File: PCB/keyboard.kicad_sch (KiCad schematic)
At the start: 1 part, among them U1 Pico

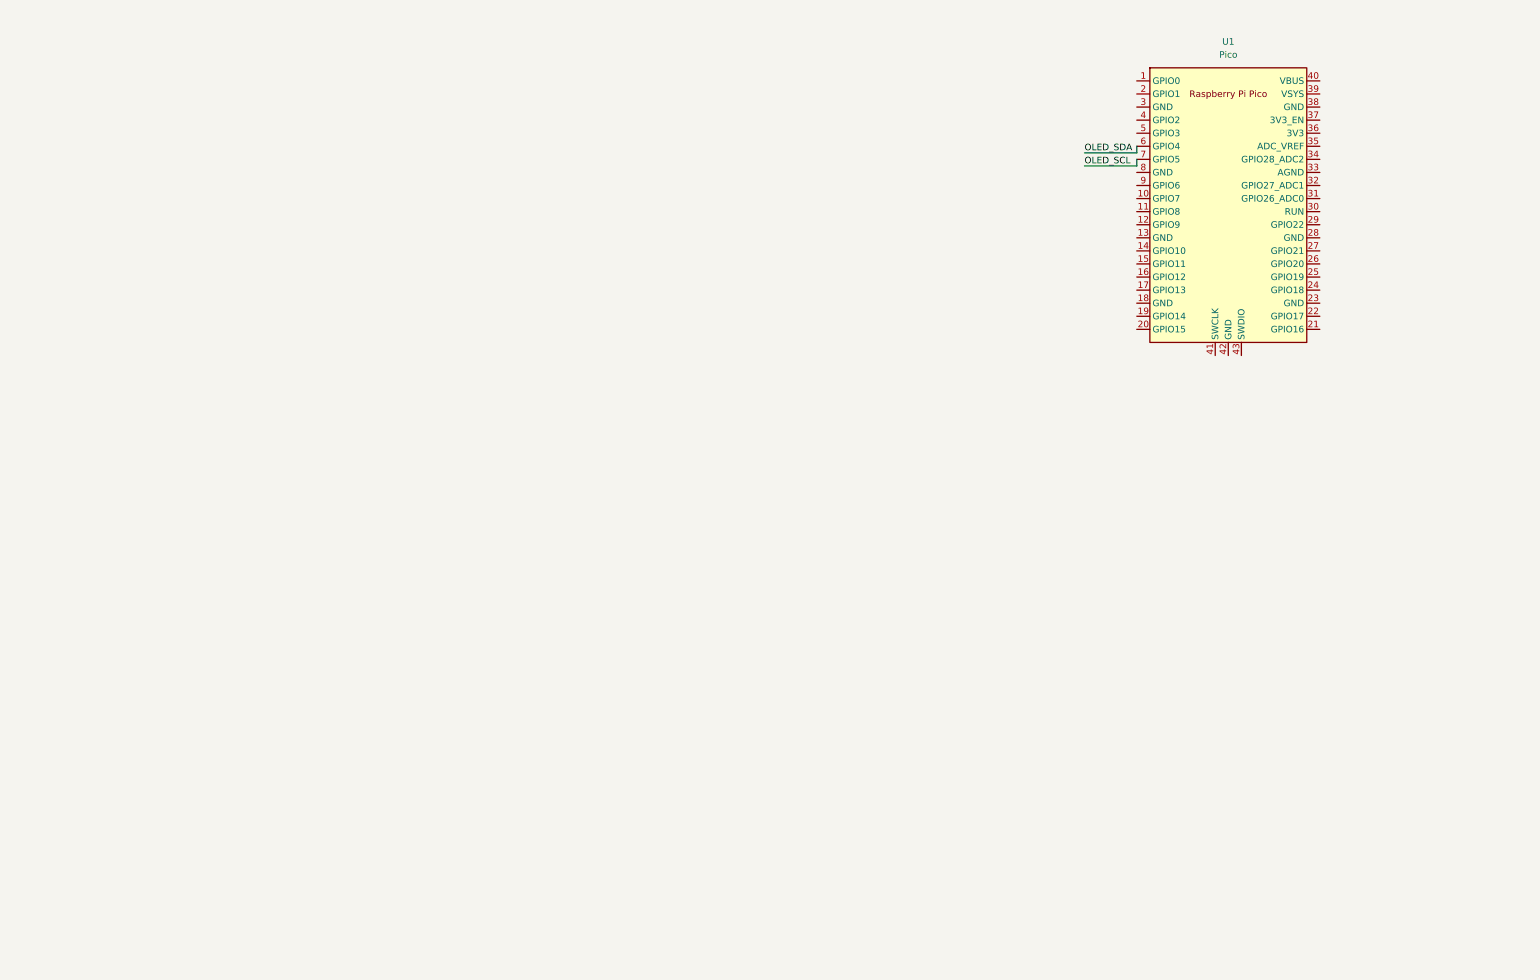
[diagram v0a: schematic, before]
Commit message: Major PCB Updates (Read desc.)
Since the last update, I designed an ANSI TKL based keyboard layout schematic in KiCad using a Raspberry Pi Pico 2W as the controller. I started by selecting and labeling usable GPIO pins on the Pico and assigning them to six row lines (ROW0–ROW5) and fifteen column lines (COL0–COL14). I had some issues figuring out diode orientation, but I got it eventually. I then expanded it into a full ANSI-based TKL layout.
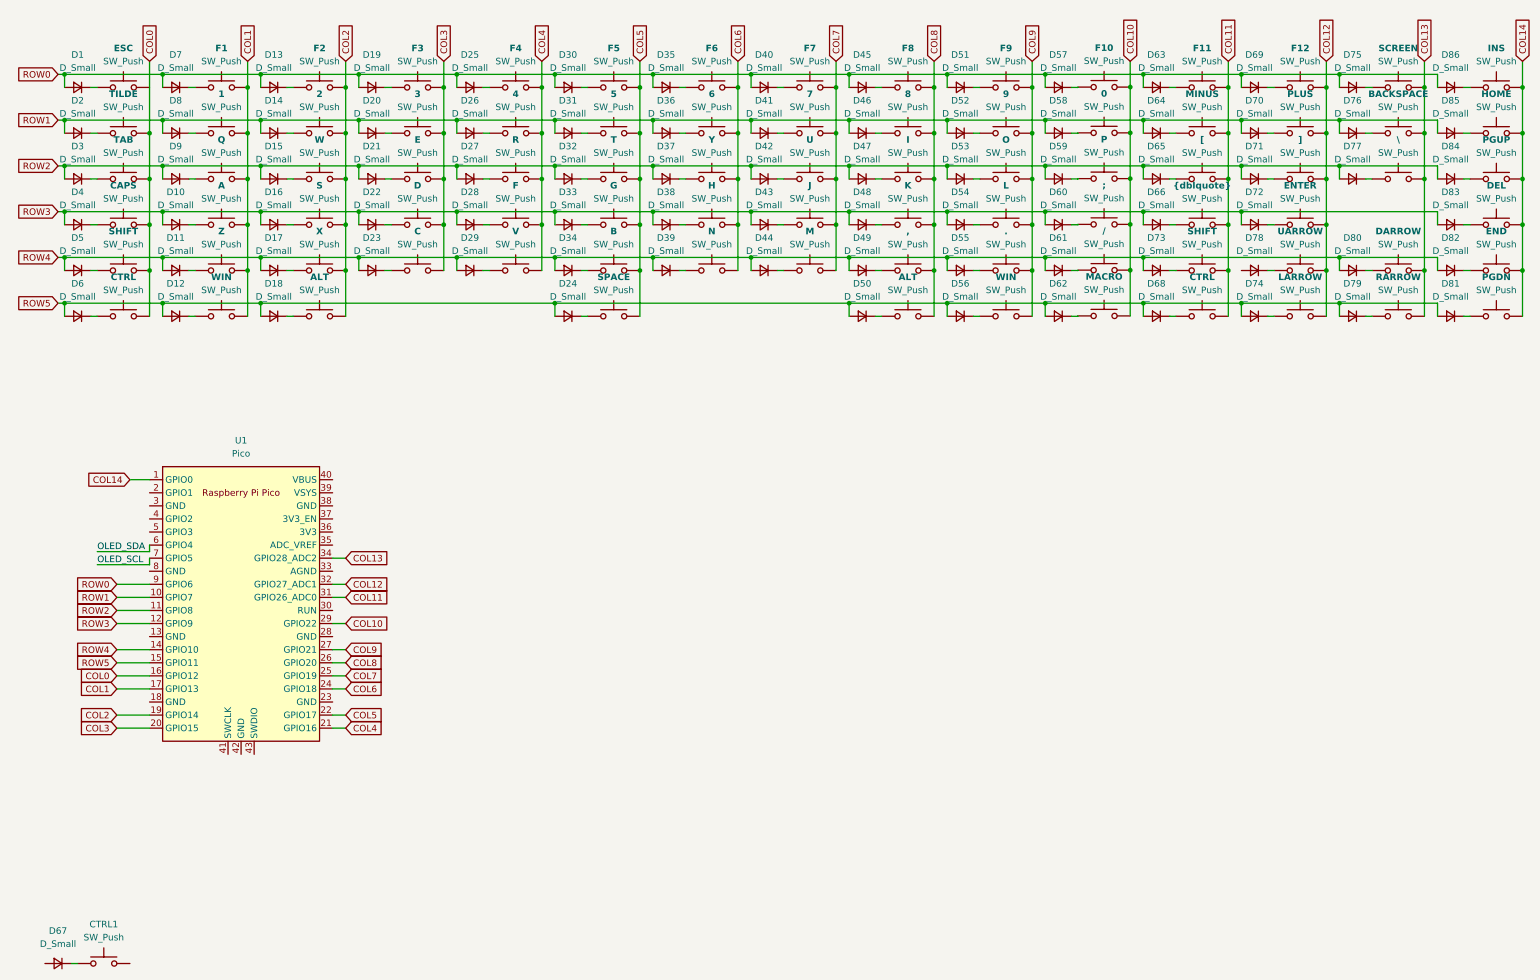
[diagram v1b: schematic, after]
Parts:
- added ,, ., /, 0, 1, 2, 3, 4, 5, 6, 7, 8, 9, ;, A, ALT (x2), B, BACKSPACE, C, CAPS, CTRL (x2), CTRL1, D, DARROW, DEL, E, END, ENTER, ESC, F, F1, F10, F11, F12, F2, F3, F4, F5, F6, F7, F8, F9, G, H, HOME, I, INS, J, K, L, LARROW, M, MACRO, MINUS, N, O, P, PGDN, PGUP, PLUS, Q, R, RARROW, S, SCREEN, SHIFT (x2), SPACE, T, TAB, TILDE, U, UARROW, V, W, WIN (x2), X, Y, Z, [, \, ], {dblquote}: SW_Push, symbol Switch:SW_Push
- added D1, D10, D11, D12, D13, D14, D15, D16, D17, D18, D19, D2, D20, D21, D22, D23, D24, D25, D26, D27, D28, D29, D3, D30, D31, D32, D33, D34, D35, D36, D37, D38, D39, D4, D40, D41, D42, D43, D44, D45, D46, D47, D48, D49, D5, D50, D51, D52, D53, D54, D55, D56, D57, D58, D59, D6, D60, D61, D62, D63, D64, D65, D66, D67, D68, D69, D7, D70, D71, D72, D73, D74, D75, D76, D77, D78, D79, D8, D80, D81, D82, D83, D84, D85, D86, D9: D_Small, symbol Device:D_Small
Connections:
- net COL14: now reaches U1.1 (GPIO0)
- net COL14: now also DEL.2, END.2, HOME.2, INS.2, PGDN.2, PGUP.2
- net ROW1: now reaches U1.10 (GPIO7)
- net ROW1: now also D14.2 (A), D2.2 (A), D20.2 (A), D26.2 (A), D31.2 (A), D36.2 (A), D41.2 (A), D46.2 (A), D52.2 (A), D58.2 (A), D64.2 (A), D70.2 (A), D76.2 (A), D8.2 (A), D85.2 (A)
- net ROW2: now reaches U1.11 (GPIO8)
- net ROW2: now also D15.2 (A), D21.2 (A), D27.2 (A), D3.2 (A), D32.2 (A), D37.2 (A), D42.2 (A), D47.2 (A), D53.2 (A), D59.2 (A), D65.2 (A), D71.2 (A), D77.2 (A), D84.2 (A), D9.2 (A)
- net ROW3: now reaches U1.12 (GPIO9)
- net ROW3: now also D10.2 (A), D16.2 (A), D22.2 (A), D28.2 (A), D33.2 (A), D38.2 (A), D4.2 (A), D43.2 (A), D48.2 (A), D54.2 (A), D60.2 (A), D66.2 (A), D72.2 (A), D83.2 (A)
- net ROW4: now reaches U1.14 (GPIO10)
- net ROW4: now also D11.2 (A), D17.2 (A), D23.2 (A), D29.2 (A), D34.2 (A), D39.2 (A), D44.2 (A), D49.2 (A), D5.2 (A), D55.2 (A), D61.2 (A), D73.2 (A), D80.2 (A), D82.2 (A)
- net ROW5: now reaches U1.15 (GPIO11)
- net ROW5: now also D12.2 (A), D18.2 (A), D24.2 (A), D50.2 (A), D56.2 (A), D6.2 (A), D62.2 (A), D68.2 (A), D74.2 (A), D79.2 (A), D81.2 (A)
- net COL0: now reaches U1.16 (GPIO12)
- net COL0: now also CAPS.2, CTRL.2, SHIFT.2, TAB.2, TILDE.2
- net COL1: now reaches U1.17 (GPIO13)
- net COL1: now also 1.2, A.2, F1.2, Q.2, WIN.2, Z.2
- net COL2: now reaches U1.19 (GPIO14)
- net COL2: now also 2.2, ALT.2, F2.2, S.2, W.2, X.2
- net COL3: now reaches U1.20 (GPIO15)
- net COL3: now also 3.2, C.2, D.2, E.2, F3.2
- net COL4: now reaches U1.21 (GPIO16)
- net COL4: now also 4.2, F.2, F4.2, R.2, V.2
- net COL5: now reaches U1.22 (GPIO17)
- net COL5: now also 5.2, B.2, F5.2, G.2, SPACE.2, T.2
- net COL6: now reaches U1.24 (GPIO18)
- net COL6: now also 6.2, F6.2, H.2, N.2, Y.2
- net COL7: now reaches U1.25 (GPIO19)
- net COL7: now also 7.2, F7.2, J.2, M.2, U.2
- net COL8: now reaches U1.26 (GPIO20)
- net COL8: now also ,.2, 8.2, ALT.2, F8.2, I.2, K.2
- net COL9: now reaches U1.27 (GPIO21)
- net COL9: now also ..2, 9.2, F9.2, L.2, O.2, WIN.2
- net COL10: now reaches U1.29 (GPIO22)
- net COL10: now also /.2, 0.2, ;.2, F10.2, MACRO.2, P.2
- net COL11: now reaches U1.31 (GPIO26_ADC0)
- net COL11: now also CTRL.2, F11.2, MINUS.2, SHIFT.2, [.2, {dblquote}.2
- net COL12: now reaches U1.32 (GPIO27_ADC1)
- net COL12: now also ENTER.2, F12.2, LARROW.2, PLUS.2, UARROW.2, ].2
- net COL13: now reaches U1.34 (GPIO28_ADC2)
- net COL13: now also BACKSPACE.2, DARROW.2, RARROW.2, SCREEN.2, \.2
- net ROW0: now reaches U1.9 (GPIO6)
- net ROW0: now also D1.2 (A), D13.2 (A), D19.2 (A), D25.2 (A), D30.2 (A), D35.2 (A), D40.2 (A), D45.2 (A), D51.2 (A), D57.2 (A), D63.2 (A), D69.2 (A), D7.2 (A), D75.2 (A), D86.2 (A)
- new net: D37.1 (K), Y.1
- new net: D33.1 (K), G.1
- new net: D35.1 (K), F6.1
- new net: 8.1, D46.1 (K)
- new net: D25.1 (K), F4.1
- new net: D69.1 (K), F12.1
- new net: A.1, D10.1 (K)
- new net: D86.1 (K), INS.1
- new net: 4.1, D26.1 (K)
- new net: D43.1 (K), J.1
- new net: D44.1 (K), M.1
- new net: D74.1 (K), LARROW.1
- new net: D62.1 (K), MACRO.1
- new net: D85.1 (K), HOME.1
- new net: D71.1 (K), ].1
- new net: D30.1 (K), F5.1
- new net: D51.1 (K), F9.1
- new net: D12.1 (K), WIN.1
- new net: D15.1 (K), W.1
- new net: D39.1 (K), N.1
- new net: CAPS.1, D4.1 (K)
- new net: D47.1 (K), I.1
- new net: D84.1 (K), PGUP.1
- new net: 7.1, D41.1 (K)
- new net: 2.1, D14.1 (K)
- new net: D21.1 (K), E.1
- new net: D28.1 (K), F.1
- new net: D59.1 (K), P.1
- new net: D40.1 (K), F7.1
- new net: D53.1 (K), O.1
- new net: D73.1 (K), SHIFT.1
- new net: D75.1 (K), SCREEN.1
- new net: 6.1, D36.1 (K)
- new net: ..1, D55.1 (K)
- new net: D81.1 (K), PGDN.1
- new net: D13.1 (K), F2.1
- new net: ALT.1, D18.1 (K)
- new net: D17.1 (K), X.1
- new net: CTRL1.1, D67.1 (K)
- new net: D29.1 (K), V.1
- new net: D57.1 (K), F10.1
- new net: BACKSPACE.1, D76.1 (K)
- new net: CTRL.1, D6.1 (K)
- new net: D3.1 (K), TAB.1
- new net: D65.1 (K), [.1
- new net: D63.1 (K), F11.1
- new net: D64.1 (K), MINUS.1
- new net: D5.1 (K), SHIFT.1
- new net: D72.1 (K), ENTER.1
- new net: D32.1 (K), T.1
- new net: D80.1 (K), DARROW.1
- new net: D77.1 (K), \.1
- new net: ALT.1, D50.1 (K)
- new net: /.1, D61.1 (K)
- new net: D42.1 (K), U.1
- new net: D79.1 (K), RARROW.1
- new net: D82.1 (K), END.1
- new net: ;.1, D60.1 (K)
- new net: D48.1 (K), K.1
- new net: D70.1 (K), PLUS.1
- new net: D.1, D22.1 (K)
- new net: D11.1 (K), Z.1
- new net: D38.1 (K), H.1
- new net: D54.1 (K), L.1
- new net: D2.1 (K), TILDE.1
- new net: 0.1, D58.1 (K)
- new net: 1.1, D8.1 (K)
- new net: D27.1 (K), R.1
- new net: CTRL.1, D68.1 (K)
- new net: D9.1 (K), Q.1
- new net: ,.1, D49.1 (K)
- new net: D19.1 (K), F3.1
- new net: D24.1 (K), SPACE.1
- new net: 3.1, D20.1 (K)
- new net: D56.1 (K), WIN.1
- new net: D1.1 (K), ESC.1
- new net: D66.1 (K), {dblquote}.1
- new net: D83.1 (K), DEL.1
- new net: D7.1 (K), F1.1
- new net: 9.1, D52.1 (K)
- new net: D78.1 (K), UARROW.1
- new net: B.1, D34.1 (K)
- new net: D45.1 (K), F8.1
- new net: D16.1 (K), S.1
- new net: 5.1, D31.1 (K)
- new net: C.1, D23.1 (K)
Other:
- moved on the sheet: U1

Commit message: Fixed a ton of ERC issues
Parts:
- removed CTRL1: SW_Push, symbol Switch:SW_Push
- removed D67: D_Small, symbol Device:D_Small
- renumbered \ to BSLASH, ] to CBRACKET, ; to COLON, , to COMMA, [ to OBRACKET, . to PERIOD, {dblquote} to QUOTE, / to SLASH, ALT to rALT, CTRL to rCTRL, SHIFT to rSHIFT, WIN to rWIN
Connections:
- net COL0: now also ESC.2
- net ROW4: now also D78.2 (A)
- no-connect marks 0 -> 20

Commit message: Fixed more issues
Had to add weird number annotations to the end of each key to stop the ERC whining
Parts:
- added OLED DISPLAY1: Conn_01x04, symbol Connector_Generic:Conn_01x04
- added SW1: RotaryEncoder_Switch, symbol Device:RotaryEncoder_Switch
- renumbered A to A1, ALT to ALT1, B to B1, BACKSPACE to BACKSPACE1, BSLASH to BSLASH1, C to C1, CAPS to CAPS1, CBRACKET to CBRACKET1, COLON to COLON1, COMMA to COMMA1, CTRL to CTRL1, D to D67, DARROW to DARROW1, DEL to DEL1, E to E1, END to END1, ENTER to ENTER1, ESC to ESC1, F to F13, G to G1, H to H1, HOME to HOME1, I to I1, INS to INS1, J to J1, K to K1, L to L1, LARROW to LARROW1, M to M1, MACRO to MACRO1, MINUS to MINUS1, N to N10, O to O1, OBRACKET to OBRACKET1, P to P1, PERIOD to PERIOD1, PGDN to PGDN1, PGUP to PGUP1, PLUS to PLUS1, Q to Q1, QUOTE to QUOTE1, R to R1, RARROW to RARROW1, S to S1, SCREEN to SCREEN1, SHIFT to SHIFT1, SLASH to SLASH1, SPACE to SPACE1, T to T1, TAB to TAB1, TILDE to TILDE1, U to U2, UARROW to UARROW1, V to V1, W to W1, WIN to WIN1, X to X1, Y to Y1, Z to Z1, 0 to n0, 1 to n1, 2 to n2, 3 to n3, 4 to n4, 5 to n5, 6 to n6, 7 to n7, 8 to n8, 9 to n9, rALT to rALT1, rCTRL to rCTRL1, rSHIFT to rSHIFT1, rWIN to rWIN1
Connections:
- net OLED_SCL: now also OLED DISPLAY1.4 (Pin_4)
- net OLED_SDA: now also OLED DISPLAY1.3 (Pin_3)
- net at U1.2 (GPIO1): now also SW1.S1
- net at U1.37 (3V3_EN): now also OLED DISPLAY1.1 (Pin_1)
- net at U1.38 (GND): now also OLED DISPLAY1.2 (Pin_2), SW1.C, SW1.S2
- net at U1.4 (GPIO2): now also SW1.A
- net at U1.5 (GPIO3): now also SW1.B
- no-connect marks 20 -> 15
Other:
- moved on the sheet: U1

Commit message: Reorganised keys to fit better
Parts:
- renumbered RARROW1 to DARROW1, UARROW1 to LARROW1, rCTRL1 to MACRO1, rALT1 to RARROW1, DARROW1 to UARROW1, rWIN1 to rALT1, LARROW1 to rCTRL1, MACRO1 to rWIN1
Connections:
- net COL12: now also RARROW1.2; no longer ENTER1.2
- net COL13: now also ENTER1.2
- net COL8: no longer RARROW1.2
- net ROW3: now also D50.2 (A)
- net ROW5: no longer D50.2 (A)
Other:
- moved on the sheet: D50, D72, ENTER1, RARROW1

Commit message: Layed out key matrix
This was extremely tedious and time consuming. I had to physically lay out all the keys in their correct positions on the PCB. I still haven't laid out the diodes, so that comes next. So far, I'm pretty happy with the layout I've achieved!
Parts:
- A1, ALT1, B1, BACKSPACE1, BSLASH1, C1, CAPS1, CBRACKET1, COLON1, COMMA1, CTRL1, D67, DARROW1, DEL1, E1, END1, ESC1, F1, F10, F11, F12, F13, F2, F3, F4, F5, F6, F7, F8, F9, G1, H1, HOME1, I1, INS1, J1, K1, L1, LARROW1, M1, MACRO1, MINUS1, N10, O1, OBRACKET1, P1, PERIOD1, PGDN1, PGUP1, PLUS1, Q1, QUOTE1, R1, S1, SCREEN1, SHIFT1, SLASH1, SPACE1, T1, TAB1, TILDE1, U2, UARROW1, V1, W1, WIN1, X1, Y1, Z1, n0, n1, n2, n3, n4, n5, n6, n7, n8, n9, rALT1, rCTRL1, rSHIFT1, rWIN1: footprint (none) -> Button_Switch_Keyboard:SW_Cherry_MX_1.00u_PCB
- D1, D10, D11, D12, D13, D14, D15, D16, D17, D18, D19, D2, D20, D21, D22, D23, D24, D25, D26, D27, D28, D29, D3, D30, D31, D32, D33, D34, D35, D36, D37, D38, D39, D4, D40, D41, D42, D43, D44, D45, D46, D47, D48, D49, D5, D50, D51, D52, D53, D54, D55, D56, D57, D58, D59, D6, D60, D61, D62, D63, D64, D65, D66, D68, D69, D7, D70, D71, D72, D73, D74, D75, D76, D77, D78, D79, D8, D80, D81, D82, D83, D84, D85, D86, D9: footprint (none) -> Diode_SMD:D_SOD-123
- ENTER1: renamed from RARROW1; footprint (none) -> Button_Switch_Keyboard:SW_Cherry_MX_1.00u_PCB
- OLED DISPLAY1: footprint (none) -> Connector_PinHeader_2.54mm:PinHeader_1x04_P2.54mm_Vertical
- RARROW1: renamed from ENTER1; footprint (none) -> Button_Switch_Keyboard:SW_Cherry_MX_1.00u_PCB
- SW1: footprint (none) -> Rotary_Encoder:RotaryEncoder_Alps_EC11E-Switch_Vertical_H20mm
- U1: footprint RPi_Pico:RPi_Pico_SMD_TH -> MCU_RaspberryPi_and_Boards:RPi_Pico_SMD_TH

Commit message: Got rid of extra unnecessary key
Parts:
- removed D75: D_Small, Diode_SMD:D_SOD-123, symbol Device:D_Small
- removed SCREEN1: SW_Push, Button_Switch_Keyboard:SW_Cherry_MX_1.00u_PCB, symbol Switch:SW_Push
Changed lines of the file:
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@@
 	)
 	(junction
-		(at 285.75 25.4)
-		(diameter 0)
-		(color 0 0 0 0)
-	)
-	(junction
 		(at 285.75 60.96)
 		(diameter 0)
@@
 	)
 	(junction
-		(at 269.24 22.86)
-		(diameter 0)
-		(color 0 0 0 0)
-	)
-	(junction
 		(at 266.7 25.4)
 		(diameter 0)
@@
 	(wire
 		(pts
-			(xy 250.19 22.86) (xy 269.24 22.86)
-		)
-		(stroke
-			(width 0)
-			(type default)
-		)
-	)
-	(wire
-		(pts
 			(xy 64.77 43.18) (xy 66.04 43.18)
 		)
@@
 	(wire
 		(pts
-			(xy 285.75 25.4) (xy 285.75 34.29)
-		)
-		(stroke
-			(width 0)
-			(type default)
-		)
-	)
-	(wire
-		(pts
 			(xy 212.09 22.86) (xy 212.09 25.4)
 		)
@@
 	(wire
 		(pts
-			(xy 269.24 22.86) (xy 288.29 22.86)
+			(xy 250.19 22.86) (xy 288.29 22.86)
 		)
 		(stroke
@@
 	(wire
 		(pts
-			(xy 269.24 22.86) (xy 269.24 25.4)
-		)
-		(stroke
-			(width 0)
-			(type default)
-		)
-	)
-	(wire
-		(pts
 			(xy 21.59 22.86) (xy 40.64 22.86)
 		)
@@
 	(wire
 		(pts
-			(xy 285.75 20.32) (xy 285.75 25.4)
+			(xy 285.75 20.32) (xy 285.75 34.29)
 		)
 		(stroke
@@
 	(wire
 		(pts
-			(xy 274.32 25.4) (xy 275.59 25.4)
-		)
-		(stroke
-			(width 0)
-			(type default)
-		)
-	)
-	(wire
-		(pts
 			(xy 57.15 20.32) (xy 57.15 25.4)
 		)
@@
 	(symbol
 		(lib_id "Switch:SW_Push")
-		(at 280.67 25.4 0)
-		(unit 1)
-		(exclude_from_sim no)
-		(in_bom yes)
-		(on_board yes)
-		(dnp no)
-		(fields_autoplaced yes)
-		(property "Reference" "SCREEN1"
-			(at 280.67 17.78 0)
-			(effects
-				(font
-					(size 1.27 1.27)
-					(thickness 0.254)
-					(bold yes)
-					(color 54 47 255 1)
-				)
-			)
-		)
-		(property "Value" "SW_Push"
-			(at 280.67 20.32 0)
-			(effects
-				(font
-					(size 1.27 1.27)
-				)
-			)
-		)
-		(property "Footprint" "Button_Switch_Keyboard:SW_Cherry_MX_1.00u_PCB"
-			(at 280.67 20.32 0)
-			(effects
-				(font
-					(size 1.27 1.27)
-				)
-				(hide yes)
-			)
-		)
-		(property "Datasheet" "~"
-			(at 280.67 20.32 0)
-			(effects
-				(font
-					(size 1.27 1.27)
-				)
-				(hide yes)
-			)
-		)
-		(property "Description" "Push button switch, generic, two pins"
-			(at 280.67 25.4 0)
-			(effects
-				(font
-					(size 1.27 1.27)
-				)
-				(hide yes)
-			)
-		)
-		(pin "1"
-		)
-		(pin "2"
-		)
-		(instances
-			(project "keyboard"
-				(path "/865a014f-22d3-4b82-bacd-05623a0d23ab"
-					(reference "SCREEN1")
-					(unit 1)
-				)
-			)
-		)
-	)
-	(symbol
-		(lib_id "Switch:SW_Push")
 		(at 147.32 34.29 0)
 		(unit 1)
@@
 					(unit 1)
 				)
-			)
-		)
-	)
-	(symbol
-		(lib_id "Device:D_Small")
-		(at 271.78 25.4 180)
-		(unit 1)
-		(exclude_from_sim no)
-		(in_bom yes)
-		(on_board yes)
-		(dnp no)
-		(fields_autoplaced yes)
-		(property "Reference" "D75"
-			(at 271.78 19.05 0)
-			(effects
-				(font
-					(size 1.27 1.27)
-				)
-			)
-		)
-		(property "Value" "D_Small"
-			(at 271.78 21.59 0)
-			(effects
-				(font
-					(size 1.27 1.27)
-				)
-			)
-		)
-		(property "Footprint" "Diode_SMD:D_SOD-123"
-			(at 271.78 25.4 90)
-			(effects
-				(font
-					(size 1.27 1.27)
-				)
-				(hide yes)
-			)
-		)
-		(property "Datasheet" "~"
-			(at 271.78 25.4 90)
-			(effects
-				(font
-					(size 1.27 1.27)
-				)
-				(hide yes)
-			)
-		)
-		(property "Description" "Diode, small symbol"
-			(at 271.78 25.4 0)
-			(effects
-				(font
-					(size 1.27 1.27)
-				)
-				(hide yes)
-			)
-		)
-		(property "Sim.Device" "D"
-			(at 271.78 25.4 0)
-			(effects
-				(font
-					(size 1.27 1.27)
-				)
-				(hide yes)
-			)
-		)
-		(property "Sim.Pins" "1=K 2=A"
-			(at 271.78 25.4 0)
-			(effects
-				(font
-					(size 1.27 1.27)
-				)
-				(hide yes)
-			)
-		)
-		(pin "2"
-		)
-		(pin "1"
-		)
-		(instances
-			(project "keyboard"
-				(path "/865a014f-22d3-4b82-bacd-05623a0d23ab"
-					(reference "D75")
-					(unit 1)
-				)
